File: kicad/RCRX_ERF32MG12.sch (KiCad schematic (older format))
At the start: 74 parts

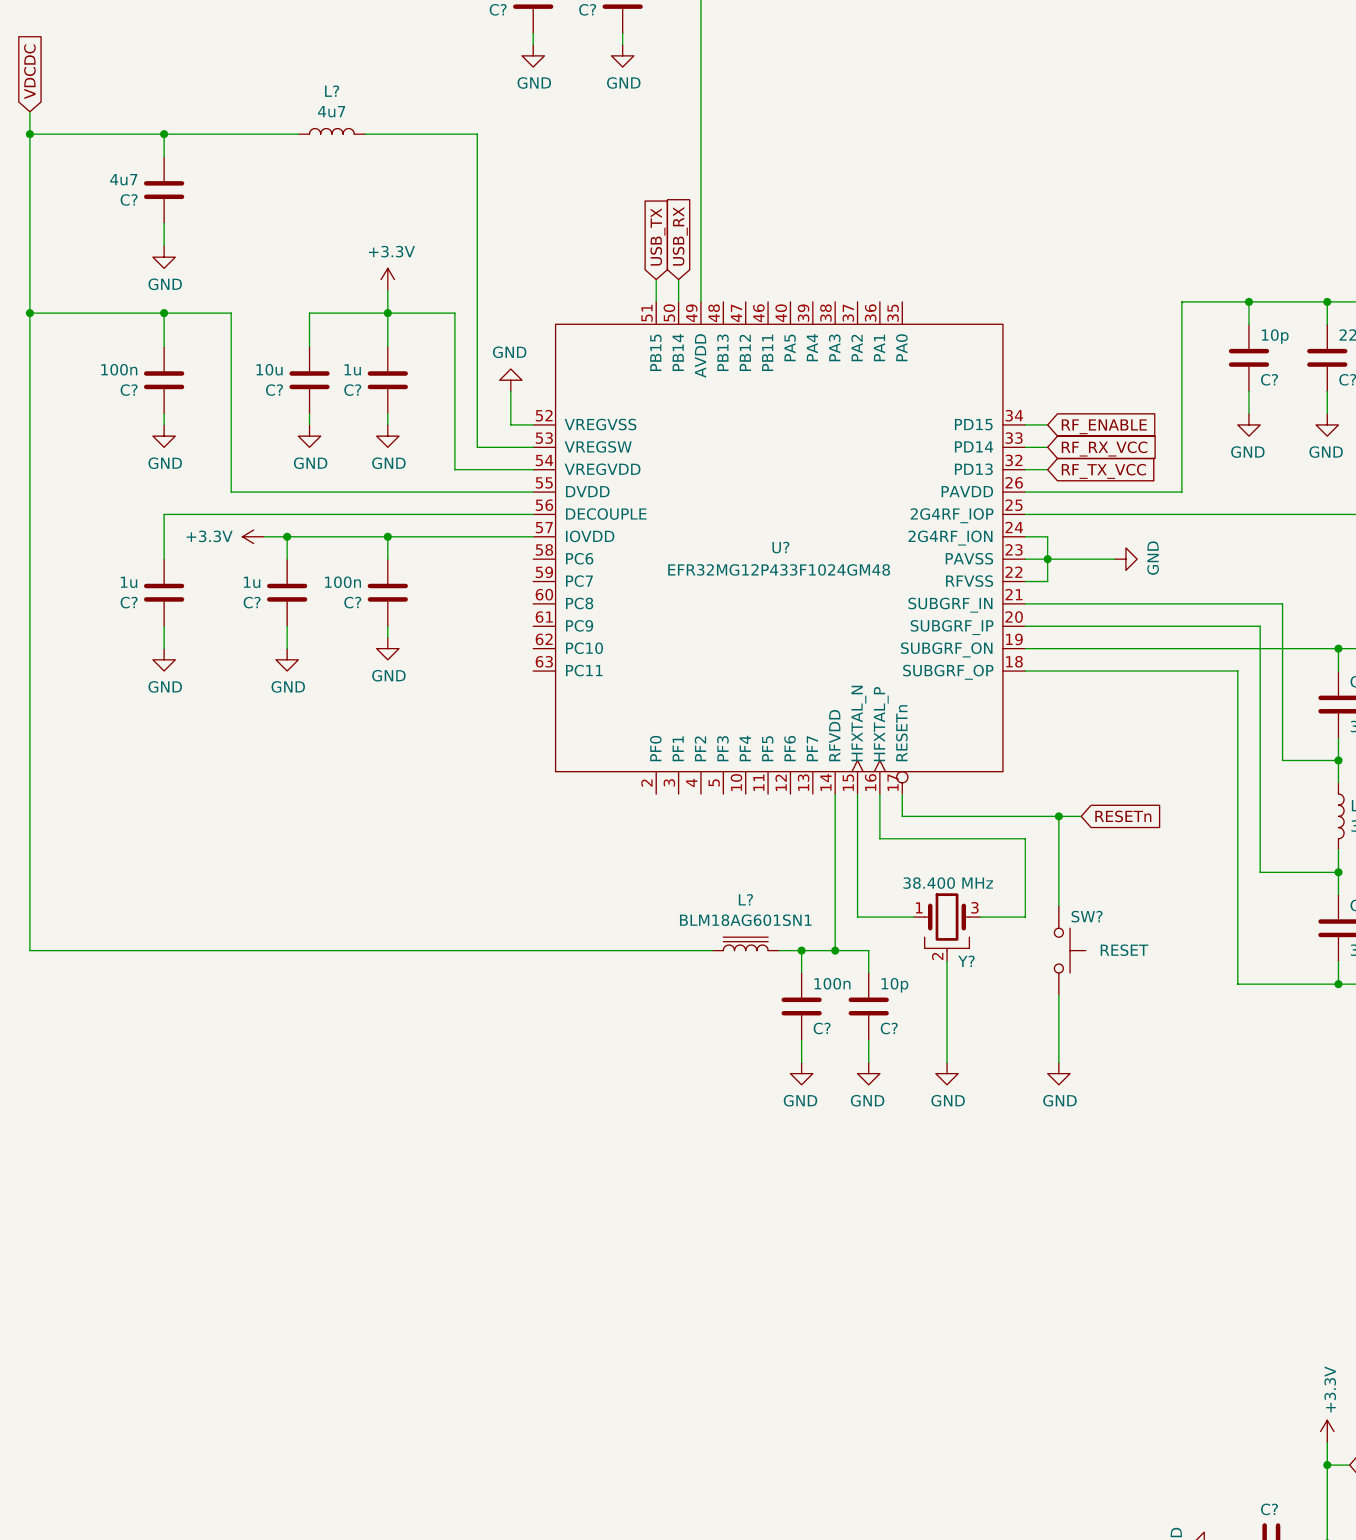
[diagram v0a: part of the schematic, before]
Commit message: Using ERF32FG12 SoC instead of PIC32MX
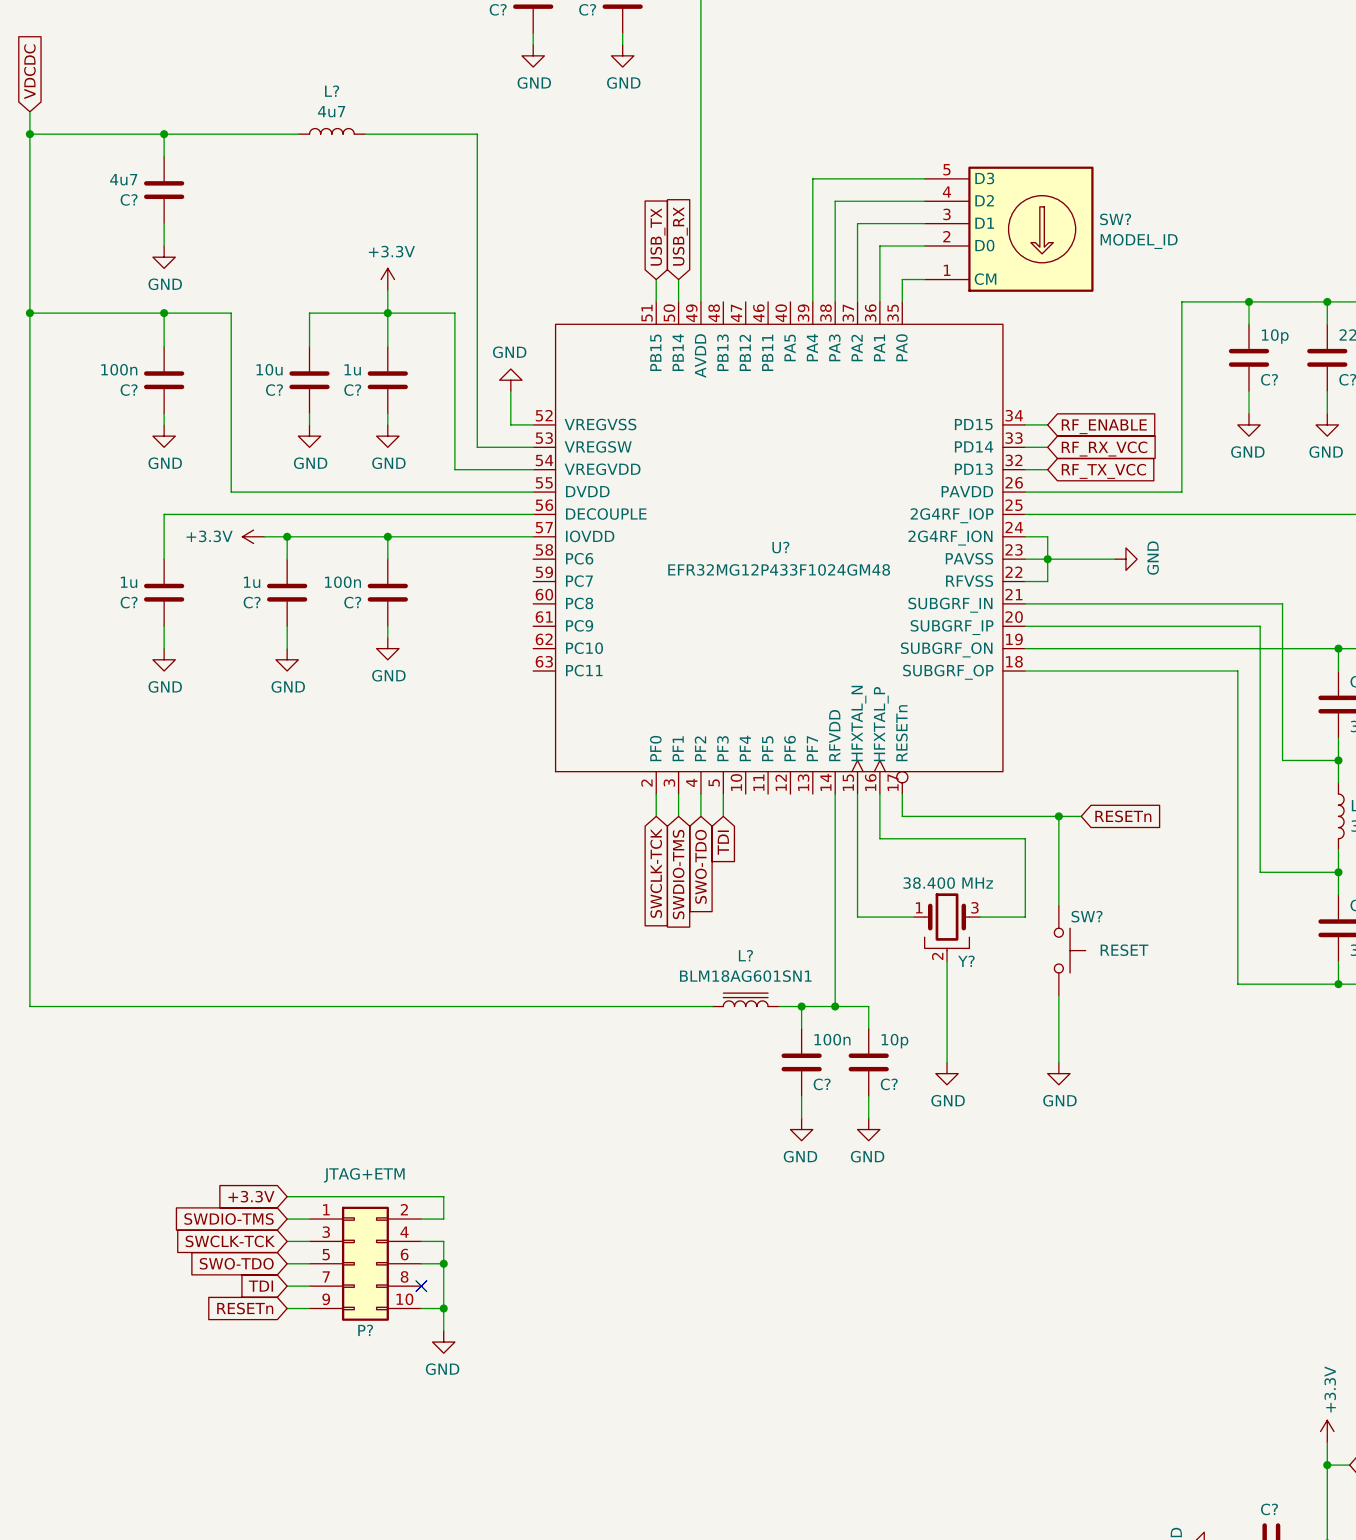
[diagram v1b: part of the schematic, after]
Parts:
- added P?: JTAG+ETM, symbol conn:Conn_02x05_Odd_Even
- added SW?: MODEL_ID, symbol switches:SW_Coded
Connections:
- net labels added: SWCLK-TCK, SWDIO-TMS, SWO-TDO, TDI
- wire segments 266 -> 294
- no-connect marks 12 -> 13
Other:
- moved on the sheet: C?, L?
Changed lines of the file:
@@
 	1950 3150 1950 3250
 Wire Wire Line
-	1350 3550 1350 6400
+	1350 3550 1350 6650
 Wire Wire Line
 	1950 3700 1950 3550
@@
 L device:L_Core_Iron L?
 U 1 1 67B075ED
-P 4550 6400
-F 0 "L?" V 4775 6400 50  0000 C CNN
-F 1 "BLM18AG601SN1" V 4684 6400 50  0000 C CNN
-F 2 "" H 4550 6400 50  0001 C CNN
-F 3 "" H 4550 6400 50  0001 C CNN
-	1    4550 6400
+P 4550 6650
+F 0 "L?" V 4775 6650 50  0000 C CNN
+F 1 "BLM18AG601SN1" V 4684 6650 50  0000 C CNN
+F 2 "" H 4550 6650 50  0001 C CNN
+F 3 "" H 4550 6650 50  0001 C CNN
+	1    4550 6650
 	0    1    -1   0
 $EndComp
@@
 	5800 5050 7200 5050
 Wire Wire Line
-	4800 6900 4800 6800
-Wire Wire Line
-	5100 6900 5100 6800
+	4800 7150 4800 7050
+Wire Wire Line
+	5100 7150 5100 7050
 $Comp
 L power:GND #PWR?
 U 1 1 69E6D570
+P 4800 7150
+F 0 "#PWR?" H 4800 6900 50  0001 C CNN
+F 1 "GND" H 4805 6977 50  0000 C CNN
+F 2 "" H 4800 7150 50  0001 C CNN
+F 3 "" H 4800 7150 50  0001 C CNN
+	1    4800 7150
+	-1   0    0    -1
+$EndComp
+$Comp
+L power:GND #PWR?
+U 1 1 69E6D576
+P 5100 7150
+F 0 "#PWR?" H 5100 6900 50  0001 C CNN
+F 1 "GND" H 5105 6977 50  0000 C CNN
+F 2 "" H 5100 7150 50  0001 C CNN
+F 3 "" H 5100 7150 50  0001 C CNN
+	1    5100 7150
+	-1   0    0    -1
+$EndComp
+Wire Wire Line
+	5100 6650 5100 6750
+$Comp
+L device:C C?
+U 1 1 69E6D57E
+P 5100 6900
+F 0 "C?" H 5150 7000 50  0000 L CNN
+F 1 "10p" H 5150 6800 50  0000 L CNN
+F 2 "" H 5138 6750 50  0001 C CNN
+F 3 "" H 5100 6900 50  0001 C CNN
+	1    5100 6900
+	1    0    0    1
+$EndComp
+$Comp
+L device:C C?
+U 1 1 69E6D584
 P 4800 6900
-F 0 "#PWR?" H 4800 6650 50  0001 C CNN
-F 1 "GND" H 4805 6727 50  0000 C CNN
-F 2 "" H 4800 6900 50  0001 C CNN
+F 0 "C?" H 4850 7000 50  0000 L CNN
+F 1 "100n" H 4850 6800 50  0000 L CNN
+F 2 "" H 4838 6750 50  0001 C CNN
 F 3 "" H 4800 6900 50  0001 C CNN
 	1    4800 6900
-	-1   0    0    -1
-$EndComp
-$Comp
-L power:GND #PWR?
-U 1 1 69E6D576
-P 5100 6900
-F 0 "#PWR?" H 5100 6650 50  0001 C CNN
-F 1 "GND" H 5105 6727 50  0000 C CNN
-F 2 "" H 5100 6900 50  0001 C CNN
-F 3 "" H 5100 6900 50  0001 C CNN
-	1    5100 6900
-	-1   0    0    -1
-$EndComp
-Wire Wire Line
-	5100 6400 5100 6500
-$Comp
-L device:C C?
-U 1 1 69E6D57E
-P 5100 6650
-F 0 "C?" H 5150 6750 50  0000 L CNN
-F 1 "10p" H 5150 6550 50  0000 L CNN
-F 2 "" H 5138 6500 50  0001 C CNN
-F 3 "" H 5100 6650 50  0001 C CNN
-	1    5100 6650
-	1    0    0    1
-$EndComp
-$Comp
-L device:C C?
-U 1 1 69E6D584
-P 4800 6650
-F 0 "C?" H 4850 6750 50  0000 L CNN
-F 1 "100n" H 4850 6550 50  0000 L CNN
-F 2 "" H 4838 6500 50  0001 C CNN
-F 3 "" H 4800 6650 50  0001 C CNN
-	1    4800 6650
 	1    0    0    1
 $EndComp
@@
 $EndComp
 Wire Wire Line
-	4800 6400 4800 6500
-Wire Wire Line
-	4800 6400 4950 6400
-Connection ~ 4950 6400
-Wire Wire Line
-	4950 6400 5100 6400
-Connection ~ 4800 6400
-Wire Wire Line
-	4400 6400 1350 6400
+	4800 6650 4800 6750
+Wire Wire Line
+	4800 6650 4950 6650
+Connection ~ 4950 6650
+Wire Wire Line
+	4950 6650 5100 6650
+Connection ~ 4800 6650
+Wire Wire Line
+	4400 6650 1350 6650
 Wire Wire Line
 	2950 4650 2950 4550
@@
 	4250 3400 4250 3500
 Wire Wire Line
-	4700 6400 4800 6400
+	4700 6650 4800 6650
 Wire Wire Line
 	4350 1750 4350 1850
@@
 	5050 6250 5050 5700
 Wire Wire Line
-	4950 5700 4950 6400
+	4950 5700 4950 6650
 $Comp
 L silabs_efr32:EFR32MG12P433F1024GM48 U?
@@
 	0    -1   -1   0
 $EndComp
+$Comp
+L switches:SW_Coded SW?
+U 1 1 632A11C3
+P 5850 3150
+F 0 "SW?" H 5570 3133 50  0000 R CNN
+F 1 "MODEL_ID" H 5570 3224 50  0000 R CNN
+F 2 "" H 5825 3175 50  0001 C CNN
+F 3 "" H 5825 3175 50  0001 C CNN
+	1    5850 3150
+	-1   0    0    1
+$EndComp
+Wire Wire Line
+	5350 3400 5250 3400
+Wire Wire Line
+	5250 3400 5250 3500
+Wire Wire Line
+	5350 3250 5150 3250
+Wire Wire Line
+	5150 3250 5150 3500
+Wire Wire Line
+	5350 3150 5050 3150
+Wire Wire Line
+	5050 3150 5050 3500
+Wire Wire Line
+	5350 3050 4950 3050
+Wire Wire Line
+	4950 3050 4950 3500
+Wire Wire Line
+	5350 2950 4850 2950
+Wire Wire Line
+	4850 2950 4850 3500
+$Comp
+L conn:Conn_02x05_Odd_Even P?
+U 1 1 63312A85
+P 2800 7800
+F 0 "P?" H 2850 7500 50  0000 C CNN
+F 1 "JTAG+ETM" H 2850 8200 50  0000 C CNN
+F 2 "" H 2800 7800 50  0001 C CNN
+F 3 "~" H 2800 7800 50  0001 C CNN
+	1    2800 7800
+	1    0    0    -1
+$EndComp
+Text GLabel 2500 7500 0    50   Input ~ 0
++3.3V
+Text GLabel 2500 7600 0    50   Input ~ 0
+SWDIO-TMS
+Text GLabel 2500 7700 0    50   Input ~ 0
+SWCLK-TCK
+Text GLabel 2500 7800 0    50   Input ~ 0
+SWO-TDO
+Text GLabel 2500 7900 0    50   Input ~ 0
+TDI
+Text GLabel 2500 8000 0    50   Input ~ 0
+RESETn
+Wire Wire Line
+	2500 7500 3200 7500
+Wire Wire Line
+	3200 7500 3200 7600
+Wire Wire Line
+	3200 7600 3100 7600
+Wire Wire Line
+	2600 7600 2500 7600
+Wire Wire Line
+	2600 7700 2500 7700
+Wire Wire Line
+	2600 7800 2500 7800
+Wire Wire Line
+	2600 7900 2500 7900
+Wire Wire Line
+	2600 8000 2500 8000
+Text GLabel 4450 5800 3    50   Input ~ 0
+TDI
+Text GLabel 4350 5800 3    50   Input ~ 0
+SWO-TDO
+Text GLabel 4150 5800 3    50   Input ~ 0
+SWCLK-TCK
+Text GLabel 4250 5800 3    50   Input ~ 0
+SWDIO-TMS
+Wire Wire Line
+	4450 5800 4450 5700
+Wire Wire Line
+	4350 5800 4350 5700
+Wire Wire Line
+	4250 5700 4250 5800
+Wire Wire Line
+	4150 5700 4150 5800
+$Comp
+L power:GND #PWR?
+U 1 1 63458EEC
+P 3200 8100
+F 0 "#PWR?" H 3200 7850 50  0001 C CNN
+F 1 "GND" H 3205 7927 50  0000 C CNN
+F 2 "" H 3200 8100 50  0001 C CNN
+F 3 "" H 3200 8100 50  0001 C CNN
+	1    3200 8100
+	-1   0    0    -1
+$EndComp
+Wire Wire Line
+	3200 8100 3200 8000
+Wire Wire Line
+	3200 8000 3100 8000
+Wire Wire Line
+	3200 8000 3200 7800
+Wire Wire Line
+	3200 7800 3100 7800
+Connection ~ 3200 8000
+Wire Wire Line
+	3200 7800 3200 7700
+Wire Wire Line
+	3200 7700 3100 7700
+Connection ~ 3200 7800
+NoConn ~ 3100 7900
 $EndSCHEMATC

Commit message: Using ERF32FG12 SoC instead of PIC32MX
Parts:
- removed C?: 100n, symbol device:C
- removed D? (x2): GREEN, symbol device:LED
- removed D?: D, symbol device:D
- removed D?: RED, symbol device:LED
- removed F?: Polyfuse, symbol device:Polyfuse
- removed P?: PWR_IN, symbol conn:Conn_01x02
- removed R? (x3): 1k, symbol device:R
- added C? (x3): 4u7, symbol device:CP
- added C? (x4): 100n, symbol device:C
- added C? (x4): 1u, symbol device:C
- added P?: CH1, symbol conn:Conn_01x03
- added P?: CH2, symbol conn:Conn_01x03
- added P?: CH3, symbol conn:Conn_01x03
- added P?: CH4, symbol conn:Conn_01x03
- added P?: CH5, symbol conn:Conn_01x03
- added P?: CH6, symbol conn:Conn_01x03
- added P?: CH7, symbol conn:Conn_01x03
- added P?: CH8, symbol conn:Conn_01x03
- added P?: BATT, symbol conn:Conn_01x03
- added R?: 4k7, symbol device:R
- added R?: 10k, symbol device:R
- added U?: LM1117-5.0, symbol regul:LM1117-5.0
- added U? (x2): TLV70245_SOT23-5, TO_SOT_Packages_SMD:SOT-23-5, symbol regul:TLV70245_SOT23-5
- added U?: ULN2803A, symbol interface:ULN2803A
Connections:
- net labels added: RF_RX_EN, RF_TX_EN
- wire segments 294 -> 393
- no-connect marks 13 -> 14
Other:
- moved on the sheet: C?, J?, P?, U?

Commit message: Adding wideband (110-350 MHz) matching network
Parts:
- removed C?: 3p, symbol device:C
- removed C?: 1n, symbol device:C
- removed C? (x2): 13p, symbol device:C
- removed C?: 10p, symbol device:C
- removed J?: 50 Ohm Antenna, symbol conn:Conn_Coaxial
- removed L?: 36n, symbol device:L
- added C? (x3): 13p, symbol device:C
- added C? (x2): 5.1p, symbol device:C
- added C?: 11p, symbol device:C
- added J?: 50 Ohm 430-460 MHz Antenna, symbol conn:Conn_Coaxial
- added J?: 50 Ohm 13-79 MHz Antenna, symbol conn:Conn_Coaxial
- added L?: 390n, symbol device:L
- added L?: 220n, symbol device:L
- added L? (x2): 22n, symbol device:L
- added U?: JSW2-63DR+, symbol RF_Mixer:JSW2-63DR+
- C? (x2): value 47u -> 33p
- C? (x3): value 82u -> 75p
- P?: value CH1 -> RUDDER_UP / XTAIL_UP_LF
- P?: value CH2 -> RUDDER_DN / XTAIL_DN_RG
- P?: value CH3 -> RUDDER_LF / XTAIL_UP_RG
- P?: value CH4 -> RUDDER_RG / XTAIL_DN_LF
- P?: value CH5 -> BOW_PLANE_LF
- P?: value CH6 -> BOW_PLANE_RG
- P?: value CH7 -> SHAFT_LF
- P?: value CH8 -> SHAFT_RG
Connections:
- net labels added: RF_BAND_SEL
- wire segments 393 -> 410
- no-connect marks 14 -> 15
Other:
- note added: "Balun"
- note added: "Bias and decoupling"
- note added: "High Band harmonics suppressor\n5th order Chebyshev low\npass filter fc: 460 MHz"
- note added: "Low Band harmonics suppressor\n9th order Chebyshev low pass filter fc: 80 MHz"
- note added: "Wideband\n(110-350 MHz)\nImpedence matching"
- note removed: "Low pass filter fc: 80 MHz"
- moved on the sheet: C?, J?, L?, U?, Y?

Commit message: Adding wideband (110-350 MHz) matching network
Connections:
- wire segments 410 -> 411
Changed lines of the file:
@@
 Wire Notes Line
 	12650 5950 12650 4650
+Wire Wire Line
+	8800 2600 8800 2500
+$Comp
+L power:GND #PWR?
+U 1 1 61CE4F54
+P 8800 2600
+F 0 "#PWR?" H 8800 2350 50  0001 C CNN
+F 1 "GND" H 8805 2427 50  0000 C CNN
+F 2 "" H 8800 2600 50  0001 C CNN
+F 3 "" H 8800 2600 50  0001 C CNN
+	1    8800 2600
+	-1   0    0    -1
+$EndComp
 $EndSCHEMATC

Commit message: Using Pic16(L)F1459 as USB->(UART/SWD/I2C) bridge
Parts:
- removed C?: 100n, symbol device:C
- removed P?: JTAG+ETM, symbol conn:Conn_02x05_Odd_Even
- added C? (x4): C, symbol device:C
- added C?: 100n, symbol device:C
- added D? (x4): D, symbol device:D
- added HEX_SW?: RF_BAND_SEL, symbol switches:SW_Coded
- added K?: AZ850-x, Relays_THT:Relay_DPDT_FRT5, symbol relays:AZ850-x
- added Q?: 3SK263, TO_SOT_Packages_SMD:SOT-143, symbol transistors:3SK263
- added R? (x8): R, symbol device:R
- added T? (x2): Transformer_1P_1S, symbol device:Transformer_1P_1S
- added Y?: Crystal, symbol device:Crystal
- gave numbers to parts that had none: 1
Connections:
- net labels added: VCC
- wire segments 411 -> 479
- no-connect marks 15 -> 10
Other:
- moved on the sheet: C?, HEX_SW?, L?, P?, R?, U?

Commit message: Using Pic16(L)F1459 as USB->(UART/SWD/I2C) bridge
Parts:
- removed C? (x4): 100n, symbol device:C
- removed C?: 4u7, symbol device:CP
- removed J?: USB_OTG, symbol conn:USB_OTG
- removed R?: 4k7, symbol device:R
- removed R?: 10k, symbol device:R
- removed U?: FT232RL, Housings_SSOP:SSOP-28_5.3x10.2mm_Pitch0.65mm, symbol ftdi:FT232RL
- added C? (x2): 33p, symbol device:C
- added D?: D_Schottky, symbol device:D_Schottky
- added J?: USB_OTG, symbol conn:USB_OTG
- added Q?: Q_PMOS_DGS, symbol device:Q_PMOS_DGS
- added R?: 100k, symbol device:R
- added U?: PIC16(L)F1459-I_ML, symbol PIC_USB_BRIDGE:PIC16(L)F1459-I_ML
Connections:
- net labels added: SWCLK, SWDIO, SWO
- net labels removed: SWCLK-TCK, SWDIO-TMS, SWO-TDO, TDI
- wire segments 479 -> 478
- no-connect marks 10 -> 8
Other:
- moved on the sheet: SW?

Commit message: Adding micro SD socket in RCRX board
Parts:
- added J?: Micro_SD_Card, symbol conn:Micro_SD_Card
- added P?: I2C_BUS, symbol conn:Conn_01x04
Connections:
- net +3V3: now also J?.4 (VDD), P?.3 (Pin_3)
- net GND: now also J?.6 (VSS), J?.9 (SHIELD), P?.4 (Pin_4)
- net I2C_SDA: now reaches U?.62 (PC10)
- net I2C_SDA: now also U?.10 (SDA), P?.2 (Pin_2)
- net I2C_SCL: now reaches U?.63 (PC11)
- net I2C_SCL: now also U?.8 (SCL), P?.1 (Pin_1)
- net SDI: now reaches U?.11 (RC2)
- net SDI: now also J?.3 (CMD)
- net CLK: now reaches U?.19 (RA5)
- net CLK: now also J?.5 (CLK)
- net SDO: now reaches U?.20 (RA4)
- net SDO: now also J?.7 (DAT0)
- net CS: now reaches U?.6 (RC7)
- net CS: now also J?.2 (DAT3/CD)
- net RESETn renamed SOC_RESETn
- no-connect marks 8 -> 10
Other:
- moved on the sheet: C?, D?, J?, L?, P?, Q?, R?, SW?, U?, Y?

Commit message: Replacing Si500/Si510 clock generator with i2c controlled Si514 model
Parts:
- removed C? (x4): C, symbol device:C
- removed D? (x4): D, symbol device:D
- removed K?: AZ850-x, Relays_THT:Relay_DPDT_FRT5, symbol relays:AZ850-x
- removed Q?: 3SK263, TO_SOT_Packages_SMD:SOT-143, symbol transistors:3SK263
- removed R? (x8): R, symbol device:R
- removed T? (x2): Transformer_1P_1S, symbol device:Transformer_1P_1S
- removed Y?: Crystal, symbol device:Crystal
- removed Y?: Si500DFAD110M000 / Si511NCB110M000C, Si500D, symbol Si500D:Si500D
- added Y?: 514CCAXXXXXXCAG, Si500D, symbol Si500D:Si514
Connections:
- net +3V3: now also Y?.6 (VDD)
- net GND: now also U?.1 (LO1), Y?.3 (GND); no longer U?.6 (LO2)
- net I2C_SCL: now also Y?.2 (SCL)
- net I2C_SDA: now also Y?.1 (SDA)
- new net: U?.6 (LO2), Y?.4 (CLK+)
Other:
- moved on the sheet: C?, P?, U?
